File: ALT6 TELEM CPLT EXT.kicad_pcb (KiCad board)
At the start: 4 copper layers, 68 x 47.7 mm, 26 parts, among them IC1 USBLC6-2SC6, IC2 USBLC6-2SC6, IC3 USBLC6-2SC6, J1 2200301031, J2 2200301031, J3 2200301021, J4 SSQ-120-01-L-D, J5 2200301031

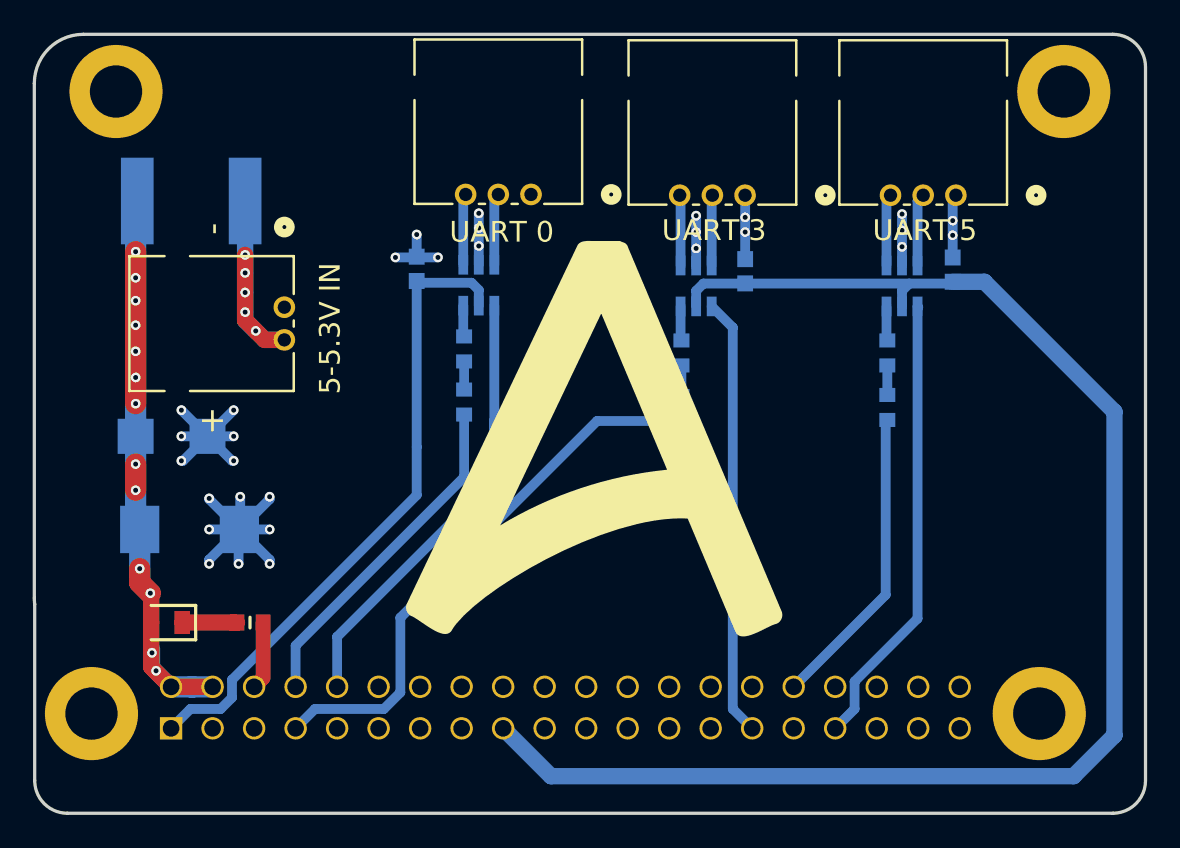
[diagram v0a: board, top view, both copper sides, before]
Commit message: Connectors change
Connectors change to vertical, improve trace design, add 0ohm in RX line to test, change the power connector (was very big and innecesary)
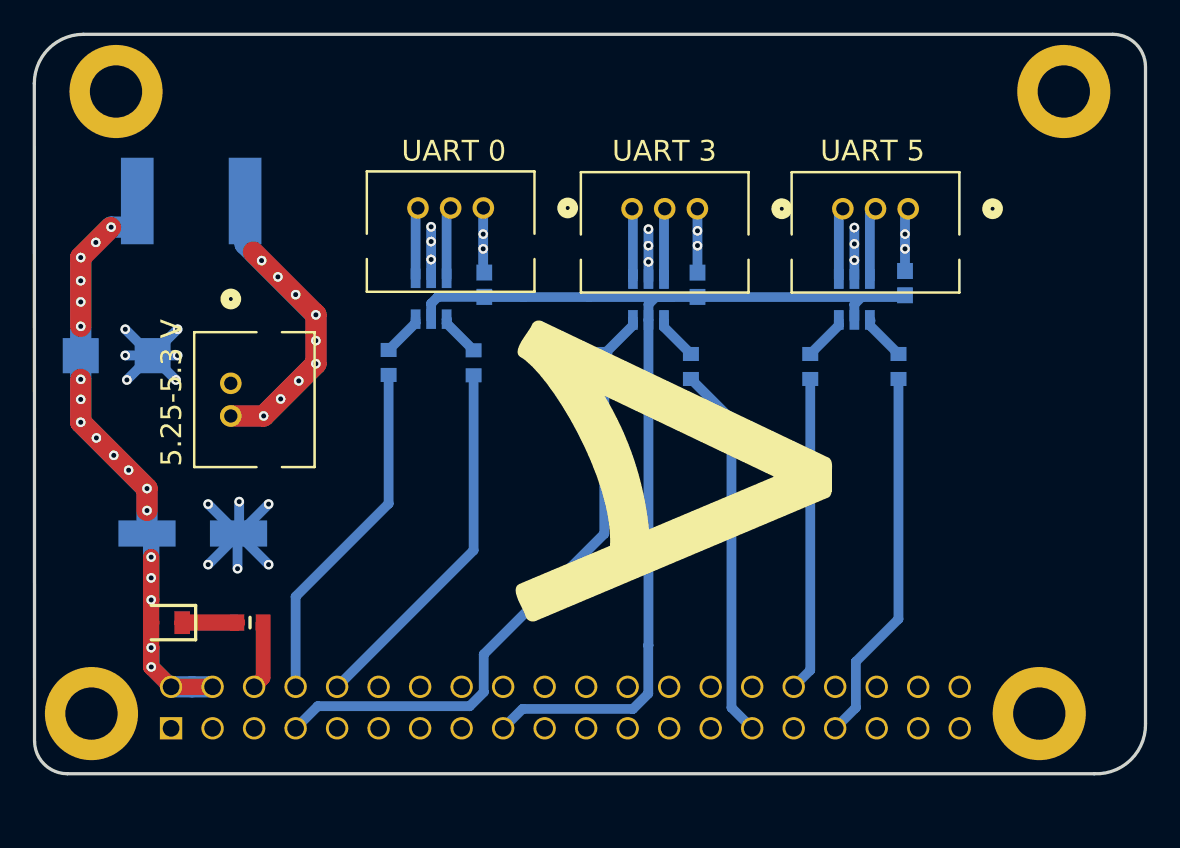
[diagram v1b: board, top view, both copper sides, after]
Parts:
- removed C3: 10TPE220ML, 10TPE220ML:16TDC150MYF
- added C5: 10SVPE220M, 10SVPE220M:CAP_10SVPE220M, B.Cu at (85.4, 146.9)
- F1: footprint 2920L600_24SLER:2920L700SLPR -> 2920L500_24SLDR:2920L700SLPR
- J1, J2, J5: value 2200301031 -> 2200291035; footprint 2200301031:CONN_2200300000-SD_03_MOL -> 2200291035:CONN_2200290000-SD_03_MOL
- J3: value 2200301021 -> 2200291025; footprint 2200301021:CONN_2200300000-SD_02_MOL -> 2200291025:CONN_2200290000-SD_02_MOL
- moved D1 5.97 mm to (80.7, 136.0)
- moved J3 5.69 mm to (87.7, 137.7)
- moved R4 4.79 mm to (123.2, 136.6)
- moved R7 4.79 mm to (110.6, 136.6)
- moved R1 4.69 mm to (97.4, 136.4)
- moved C1 4.25 mm to (103.2, 131.6)
- moved C2 3.03 mm to (129.0, 131.5)
- moved J2 3.03 mm to (129.2, 127.0)
- moved C4 3.03 mm to (116.3, 131.6)
- moved IC3 3.03 mm to (113.3, 132.5)
- moved J1 3.03 mm to (103.2, 126.9)
- moved J5 3.03 mm to (116.3, 127.0)
- moved IC1 3.03 mm to (100.0, 132.5)
- moved IC2 3.03 mm to (125.9, 132.5)
- moved R6 2.64 mm to (115.9, 136.6)
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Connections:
- C2 pad 2: Net-(IC2-VBUS) -> Net-(IC1-VBUS)
- C4 pad 2: Net-(IC2-VBUS) -> Net-(IC1-VBUS)
- IC2 pad 5: Net-(IC2-VBUS) -> Net-(IC1-VBUS)
- IC3 pad 5: Net-(IC2-VBUS) -> Net-(IC1-VBUS)
- J4 pad 01: Net-(IC1-VBUS) -> unconnected-(J4-Pad01)
- J4 pad 10: Net-(IC1-I/O2_2) -> Net-(J4-Pad10)
- J4 pad 17: Net-(IC2-VBUS) -> Net-(IC1-VBUS)
- J4 pad 29: Net-(IC3-I/O2_2) -> Net-(J4-Pad29)
- J4 pad 33: Net-(IC2-I/O2_2) -> Net-(J4-Pad33)
- R1 pad 1: Net-(R1-Pad1) -> Net-(J4-Pad08)
- R2 pad 1: Net-(J4-Pad08) -> Net-(J4-Pad10)
- R2 pad 2: Net-(R1-Pad1) -> Net-(IC1-I/O2_2)
- R3 pad 1: Net-(J4-Pad32) -> Net-(J4-Pad33)
- R3 pad 2: Net-(R3-Pad2) -> Net-(IC2-I/O2_2)
- R4 pad 1: Net-(R3-Pad2) -> Net-(J4-Pad32)
- R6 pad 1: Net-(J4-Pad07) -> Net-(J4-Pad29)
- R6 pad 2: Net-(R6-Pad2) -> Net-(IC3-I/O2_2)
- R7 pad 1: Net-(R6-Pad2) -> Net-(J4-Pad07)
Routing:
- net Net-(IC2-VBUS): track 90.7 -> 0.00 mm
- net Net-(IC1-VBUS): track 39.7 -> 66.6 mm
- net Net-(IC1-I/O2_2): track 27.8 -> 2.59 mm
- net Net-(IC2-I/O2_2): track 28.0 -> 2.87 mm
- net Net-(IC3-I/O2_2): track 26.8 -> 2.77 mm
- net Net-(J4-Pad33): track 0.00 -> 23.0 mm
- net Net-(J4-Pad29): track 0.00 -> 22.9 mm
- net Net-(J4-Pad10): track 0.00 -> 22.5 mm
- net Net-(F1-Pad2): track 18.0 -> 33.2 mm, vias 5 -> 9
- net Net-(D1-K): track 49.4 -> 59.8 mm, vias 13 -> 19
- net GND: track 56.3 -> 51.4 mm, vias 30 -> 27
- net Net-(R6-Pad2): track 1.87 -> 0.00 mm
- net Net-(R3-Pad2): track 1.86 -> 0.00 mm
- net Net-(R1-Pad1): track 1.72 -> 0.00 mm
- net Net-(J4-Pad07): track 34.1 -> 35.1 mm
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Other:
- board size 68 x 47.7 mm -> 68 x 45.2 mm

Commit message: Complete Schematic
added labels in the schematic
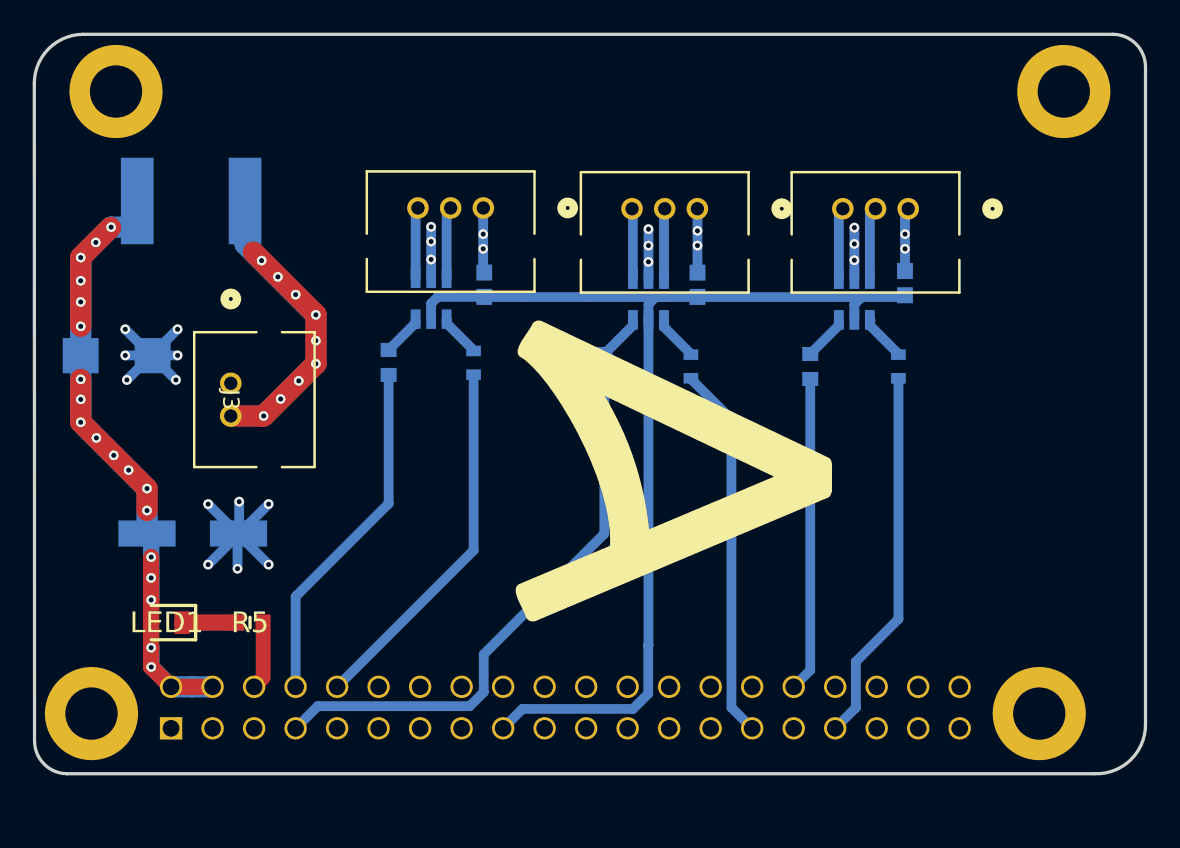
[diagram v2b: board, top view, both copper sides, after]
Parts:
- F1: footprint 2920L500_24SLDR:2920L700SLPR -> 2920L600_24SLER:2920L700SLPR
- R2, R3, R6: value CRCW060347R0FKEA -> ERJ-3GEY0R00V; footprint CRCW060347R0FKEA:RESC1508X50N -> ERJ-3GEY0R00V:RES_ERJ-3GEY0R00V

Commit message: Reupload footprints
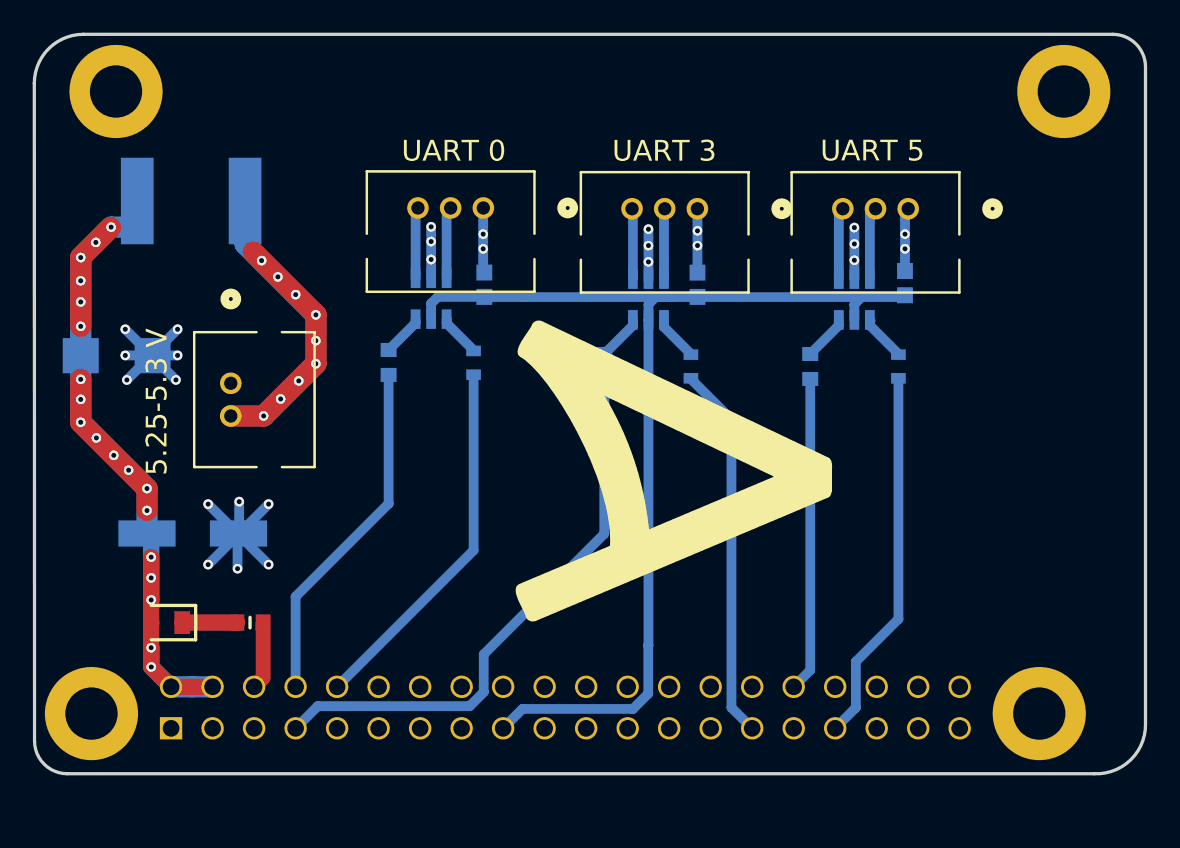
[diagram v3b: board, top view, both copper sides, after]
